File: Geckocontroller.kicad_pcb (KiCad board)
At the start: 2 copper layers, 114.3 x 96.5 mm, 94 parts, among them J101 AC Input, J11 I²C (BME280), J21 RGB LED, J31 DS18B20 I, J32 DS18B20 II, J40 Fan Connector, J51 USB-C, J61 Load Cell Connector, J70 SPI / Addon Connector, J81 Dimmer, J91 Pump, J92 HeatBed, J93 HeatLamp, K81 AQG12212, K91 AQG12112, K92 AQG12112, K93 AQG12112, Q21 AO3400A, Q22 AO3400A, Q23 AO3400A, Q51 S8050, Q52 S8050, Q61 S8550, Q81 AO3400A, Q91 AO3400A, Q92 AO3400A, Q93 AO3400A, SW1 SW_Push, U1 ESP32-WROOM-32, U101 ACT4088, U2 CP2102, U61 HX711, U81 6N138

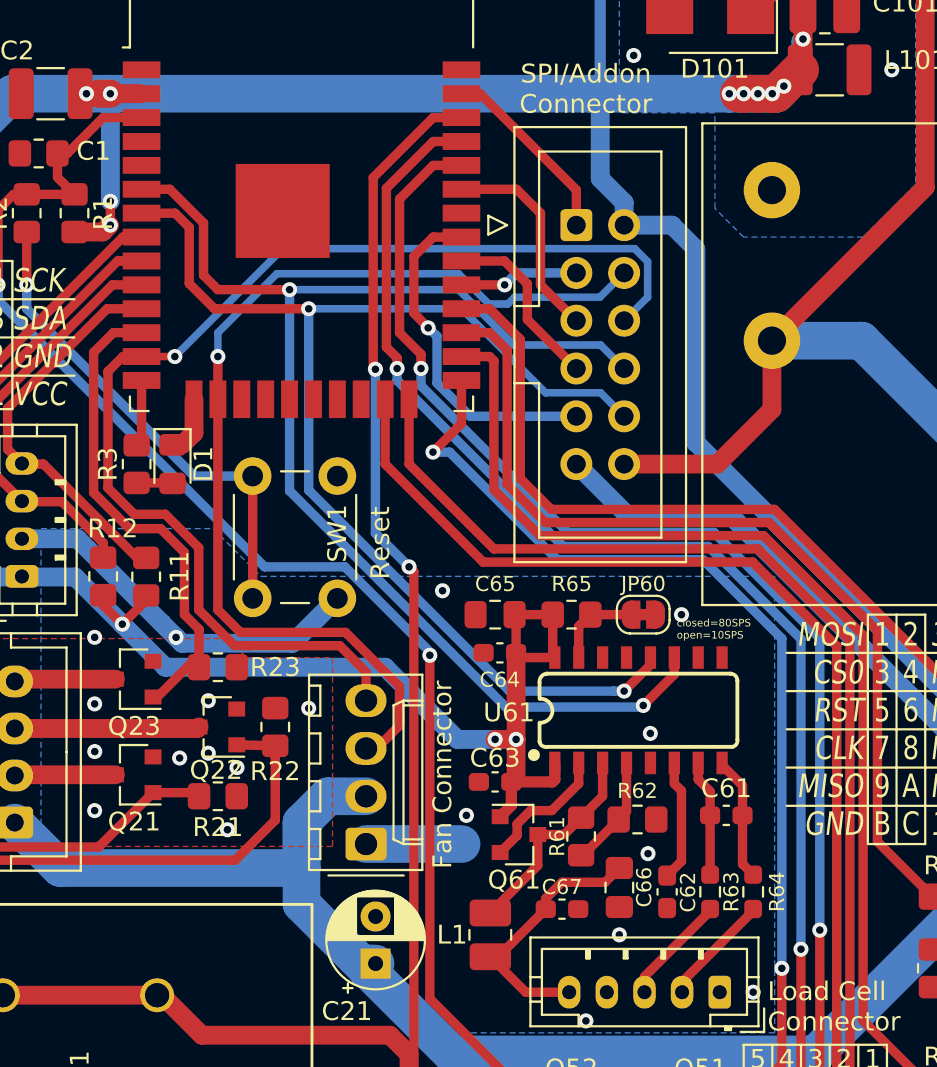
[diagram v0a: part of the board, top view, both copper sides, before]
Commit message: Schema+PCB: Switch GPIOs, add HX711 enable jumper
* GPIO34 can only be used as input,
so switch HX_CLK and FAN_SIG.
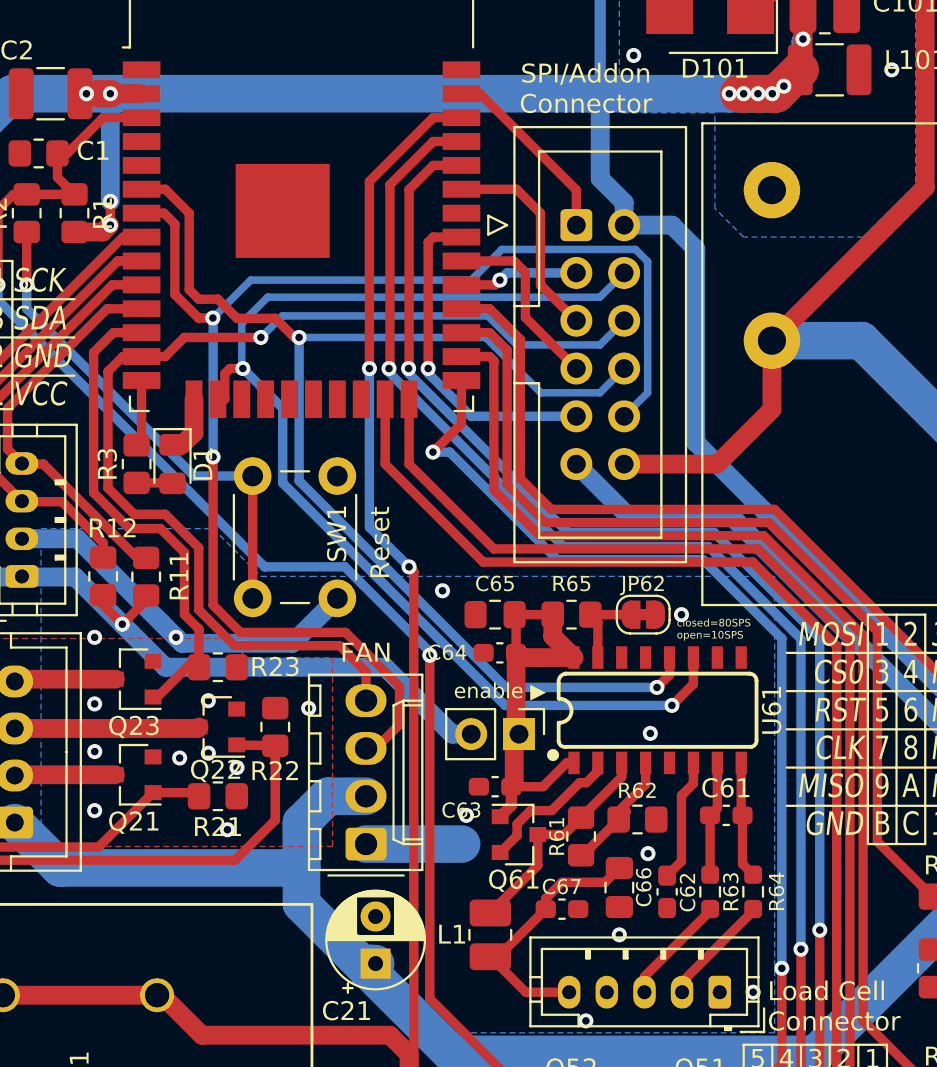
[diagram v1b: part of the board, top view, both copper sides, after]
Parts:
- added JP61: enable ▶, Connector_PinHeader_2.54mm:PinHeader_1x02_P2.54mm_Vertical, F.Cu at (49.0, 62.0)
- J40: value Fan Connector -> FAN
- moved U61 1.02 mm to (56.4, 60.7)
- moved C63 0.25 mm to (47.8, 64.8)
- renumbered J61 to J60, JP60 to JP62
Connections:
- C63 pad 1: +3V3 -> Net-(C63-Pad1)
- C64 pad 1: +3V3 -> Net-(C63-Pad1)
- C65 pad 1: +3V3 -> Net-(C63-Pad1)
- J70 pad 10: HX_DATA -> FAN_SIG
- J70 pad 4: FAN_SIG -> HX_CLK
- J70 pad 8: HX_CLK -> HX_DATA
- Q61 pad 1: +3V3 -> Net-(C63-Pad1)
- R65 pad 1: +3V3 -> Net-(C63-Pad1)
- U1 pad 16: FAN_SIG -> HX_CLK
- U1 pad 6: HX_CLK -> HX_DATA
- U1 pad 7: HX_DATA -> FAN_SIG
- U61 pad 1: +3V3 -> Net-(C63-Pad1)
- U61 pad 16: +3V3 -> Net-(C63-Pad1)
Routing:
- net +3V3: track 324.0 -> 299.6 mm, vias 19 -> 17
- net Net-(C63-Pad1): track 0.00 -> 23.2 mm
- net FAN_SIG: track 55.3 -> 73.8 mm, vias 1 -> 2
- net HX_CLK: track 69.4 -> 62.9 mm
- net FAN_PWM: track 63.5 -> 58.0 mm
- net HX_DATA: track 65.1 -> 66.8 mm
- net Net-(R61-Pad2): track 5.96 -> 6.98 mm
- net SPI_MISO: track 18.3 -> 17.7 mm
- net Net-(Q61-Pad2): track 7.15 -> 7.78 mm

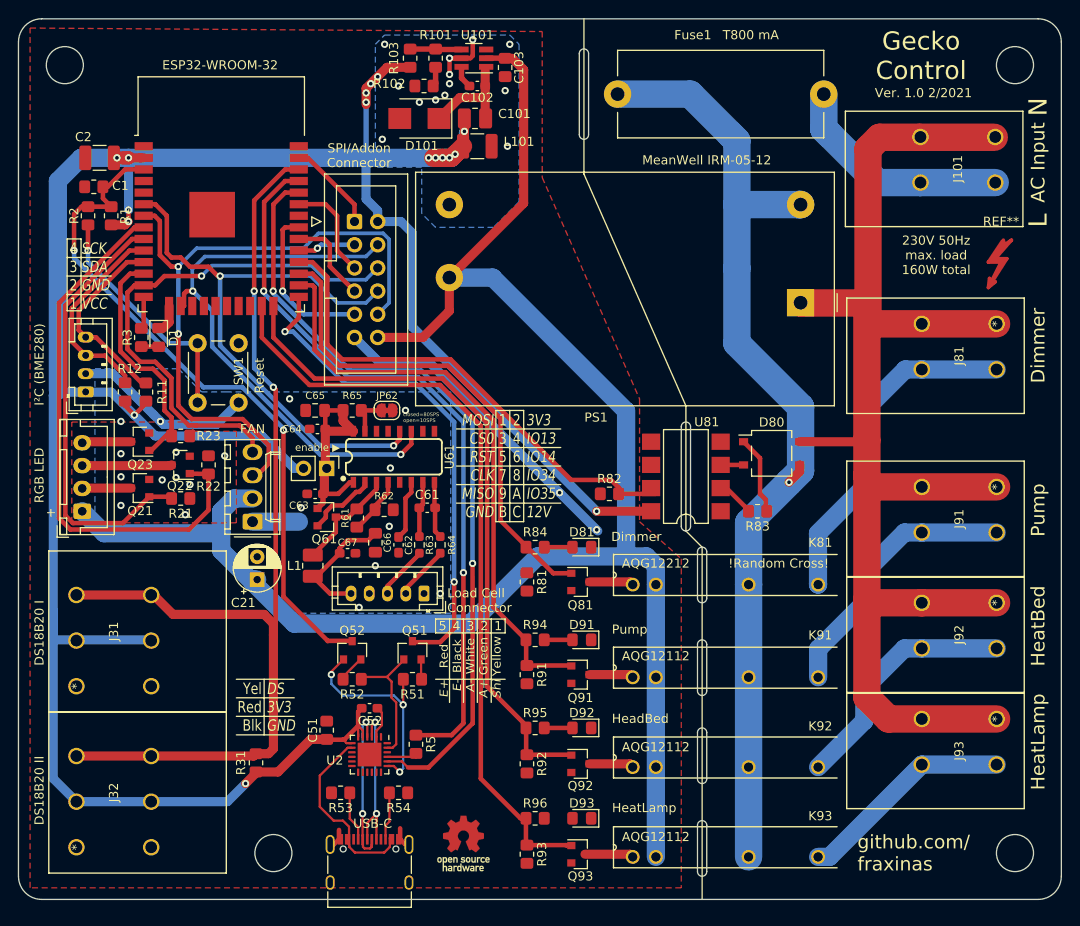
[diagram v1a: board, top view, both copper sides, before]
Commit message: Schema+PCB: Fix a few ERC issues, add warning symbols + QR Code
Mark unconnected Pins with X's, set WAGO pins to passive
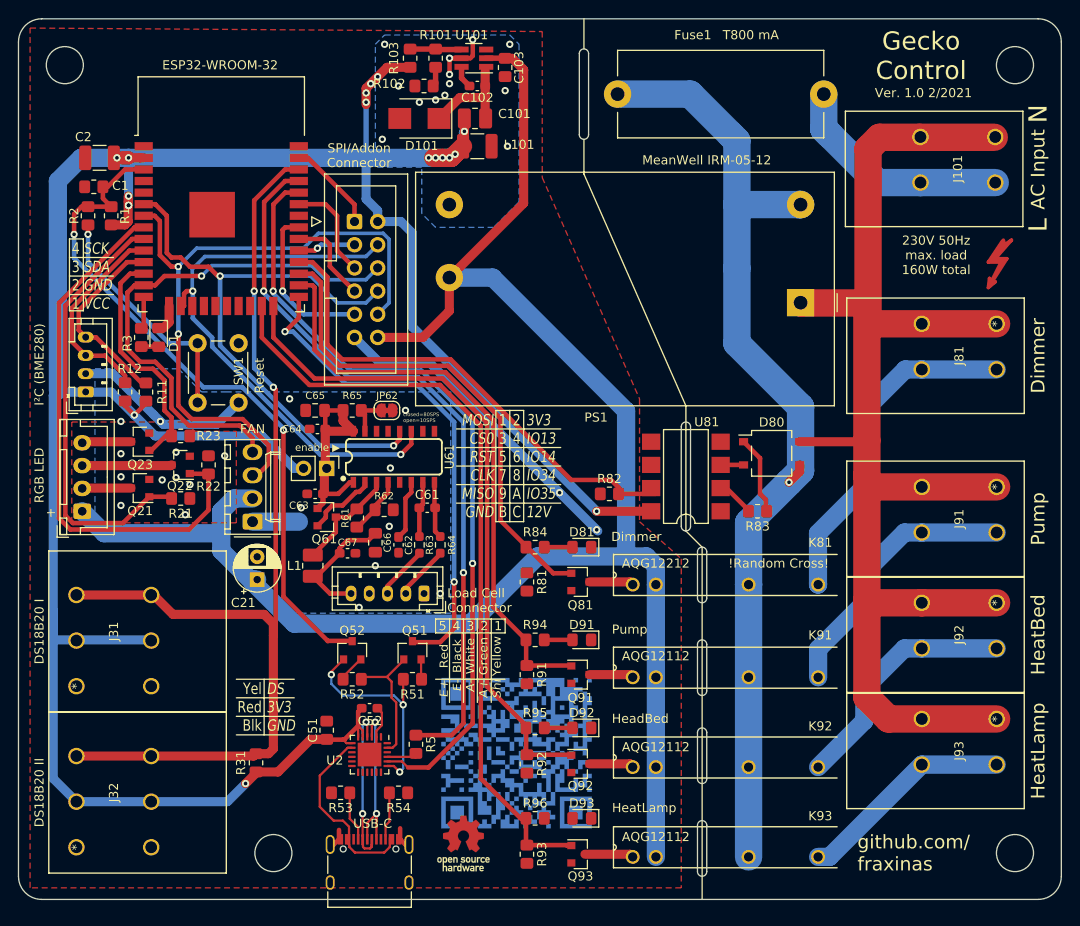
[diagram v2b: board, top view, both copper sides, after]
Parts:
- added QR*****: qr_geckocontroller, footprints:qr_geckocontroller, B.Cu at (70.1, 92.9)
- added REF**: Danger - Mains Voltage!, footprints:Symbol_Attention_SilkBack_Big, F.Cu at (100.1, 56.4)
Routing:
- net +3V3: track 299.6 -> 300.6 mm, vias 17 -> 18

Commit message: Schema+PCB: Switch CP2102 with QFN28 version, add another Switch
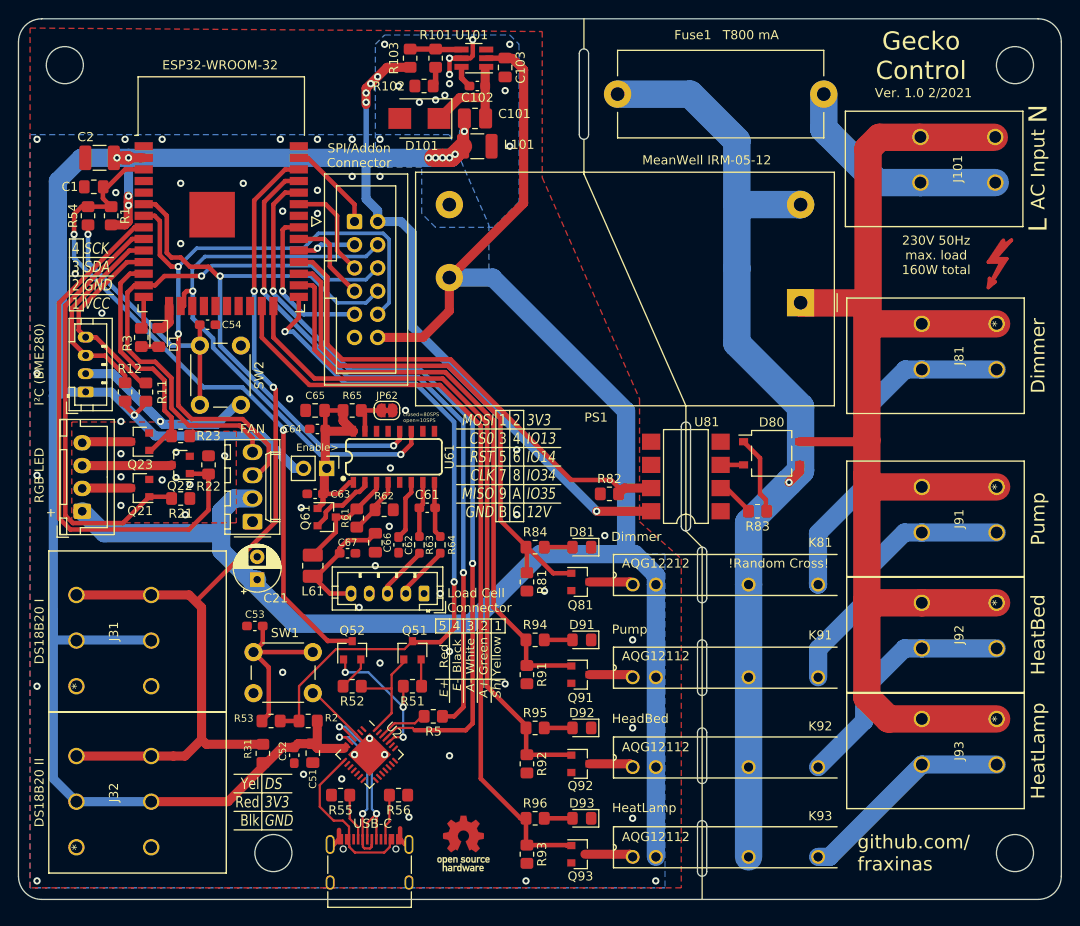
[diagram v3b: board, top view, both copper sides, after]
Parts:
- removed QR*****: qr_geckocontroller, footprints:qr_geckocontroller
- added C53: 100nF, Capacitor_SMD:C_0603_1608Metric_Pad1.08x0.95mm_HandSolder, F.Cu at (41.1, 79.2)
- added C54: 100nF, Capacitor_SMD:C_0603_1608Metric_Pad1.08x0.95mm_HandSolder, F.Cu at (36.0, 46.2)
- added R53: 470R, Resistor_SMD:R_0805_2012Metric_Pad1.20x1.40mm_HandSolder, F.Cu at (42.9, 89.7)
- added R54: 470R, Resistor_SMD:R_0805_2012Metric_Pad1.20x1.40mm_HandSolder, F.Cu at (22.9, 34.3)
- added SW2: SW_Push, Button_Switch_THT:SW_PUSH_6mm, F.Cu at (39.6, 48.5)
- C1, C103, C51: footprint Resistor_SMD:R_0805_2012Metric_Pad1.20x1.40mm_HandSolder -> Capacitor_SMD:C_0805_2012Metric_Pad1.18x1.45mm_HandSolder
- JP61: value enable ▶ -> Enable>
- R1: value 10k -> 12k
- R2: value 470R -> 12k
- U2: footprint Package_DFN_QFN:QFN-24-1EP_4x4mm_P0.5mm_EP2.6x2.6mm -> Package_DFN_QFN:QFN-28-1EP_5x5mm_P0.5mm_EP3.35x3.35mm
- moved R2 60.4 mm to (47.0, 89.7), turned to 180 degrees
- moved SW1 39.2 mm to (47.5, 86.6), turned to 180 degrees
- moved C52 9.73 mm to (45.5, 93.4), turned to 270 degrees
- moved R5 3.61 mm to (60.7, 89.2), turned to 0 degrees
- moved C51 2.94 mm to (47.5, 93.2), turned to 270 degrees
- moved R31 1.28 mm to (42.0, 93.2)
- moved R51 0.76 mm to (58.4, 85.9)
- moved R52 0.76 mm to (51.8, 85.9)
- moved R55 0.25 mm to (50.5, 97.8)
- moved R56 0.25 mm to (56.9, 97.8)
- turned U2 to 315 degrees
- renumbered L1 to L61, R53 to R55, R54 to R56
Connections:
- R2 pad 1: /Reset_switch -> +3V3
- R2 pad 2: EN -> IO0
- SW1 pad 2: /Reset_switch -> /Boot_switch
- U2 pad 19: /RTS -> (no net)
- U2 pad 2: GND -> (no net)
- U2 pad 20: RXD -> (no net)
- U2 pad 21: TXD -> (no net)
- U2 pad 23: /DTR -> (no net)
- U2 pad 24: (no net) -> /RTS
- U2 pad 25: GND -> RXD
- U2 pad 3: /D+ -> GND
- U2 pad 4: /D- -> /D+
- U2 pad 5: +3V3 -> /D-
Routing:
- net GND: track 81.3 -> 44.3 mm, vias 34 -> 73
- net IO0: track 54.9 -> 75.3 mm
- net /Boot_switch: track 0.00 -> 18.6 mm
- net /DS_in: track 114.4 -> 105.9 mm
- net /RTS: track 24.0 -> 16.8 mm
- net +3V3: track 300.6 -> 294.9 mm, vias 18 -> 16
- net /TXD': track 81.3 -> 76.6 mm
- net Net-(D93-Pad2): track 0.00 -> 3.09 mm
- net /Dimmer_out: track 54.2 -> 57.1 mm
- net /Reset_switch: track 26.3 -> 28.9 mm
- net TXD: track 3.19 -> 5.58 mm
- net /DTR: track 14.5 -> 12.4 mm
- net /VBUS: track 20.5 -> 18.5 mm
- net /D+: track 17.3 -> 19.1 mm
- net RXD: track 85.5 -> 84.3 mm
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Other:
- board text removed: "Reset"

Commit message: PCB: Add Repairfox and Purple Gecko silkscreen prints
Schema: move graphical boxes around a bit
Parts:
- added G***: LOGO, footprints:purplegecko, F.Cu at (31.2, 33.0)
- added G***: LOGO, footprints:repairfox, F.Cu at (50.5, 72.1)
